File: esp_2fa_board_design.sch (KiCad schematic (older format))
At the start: 40 parts, among them IC1 TPS22919DCKR, J1 Conn_01x06_Female, J2 USB_C_Receptacle_USB2.0, Q1 DMP2045U-7, SW1 SW_Push, SW2 SW_Push, SW3 BOOT, SW4 RESET, U1 ESP32-WROOM-32, U2 DS3231M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

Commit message: Updated schematics - removed coin cell charging circuit
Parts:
- removed D1: 1N4148, Diode_THT:D_DO-35_SOD27_P7.62mm_Horizontal, symbol esp_2fa_board_design-rescue:1N4148-Diode
- removed R4: 200, Resistor_SMD:R_2816_7142Metric_Pad3.20x4.45mm_HandSolder, symbol esp_2fa_board_design-rescue:R_Small_US-Device
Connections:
- wire segments 164 -> 160
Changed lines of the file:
@@
 $EndDescr
-$Comp
-L esp_2fa_board_design-rescue:R_Small_US-Device R4
-U 1 1 5F5143E7
-P 9650 1350
-F 0 "R4" V 9550 1350 50  0000 C CNN
-F 1 "200" V 9764 1350 50  0000 C CNN
-F 2 "Resistor_SMD:R_2816_7142Metric_Pad3.20x4.45mm_HandSolder" H 9650 1350 50  0001 C CNN
-F 3 "~" H 9650 1350 50  0001 C CNN
-	1    9650 1350
-	0    -1   -1   0
-$EndComp
 $Comp
 L esp_2fa_board_design-rescue:C-Device C2
@@
 Wire Wire Line
 	8800 1650 8800 1900
-$Comp
-L esp_2fa_board_design-rescue:1N4148-Diode D1
-U 1 1 5F5151C5
-P 9200 1350
-F 0 "D1" H 9100 1300 50  0000 C CNN
-F 1 "1N4148" H 9200 1450 50  0000 C CNN
-F 2 "Diode_THT:D_DO-35_SOD27_P7.62mm_Horizontal" H 9200 1175 50  0001 C CNN
-F 3 "https://assets.nexperia.com/documents/data-sheet/1N4148_1N4448.pdf" H 9200 1350 50  0001 C CNN
-	1    9200 1350
-	1    0    0    -1
-$EndComp
-Wire Wire Line
-	9350 1350 9550 1350
-Wire Wire Line
-	9050 1350 8800 1350
-Wire Wire Line
-	8800 1350 8800 1650
-Connection ~ 8800 1650
-Wire Wire Line
-	9950 1350 9750 1350
 Wire Wire Line
 	9550 3500 9800 3500
@@
 Text Label 7200 1300 2    50   ~ 0
 LOAD_SWITCH_VCC
-Text Label 9950 1350 0    50   ~ 0
-LOAD_SWITCH_VCC
-Wire Wire Line
+Wire Wire Line

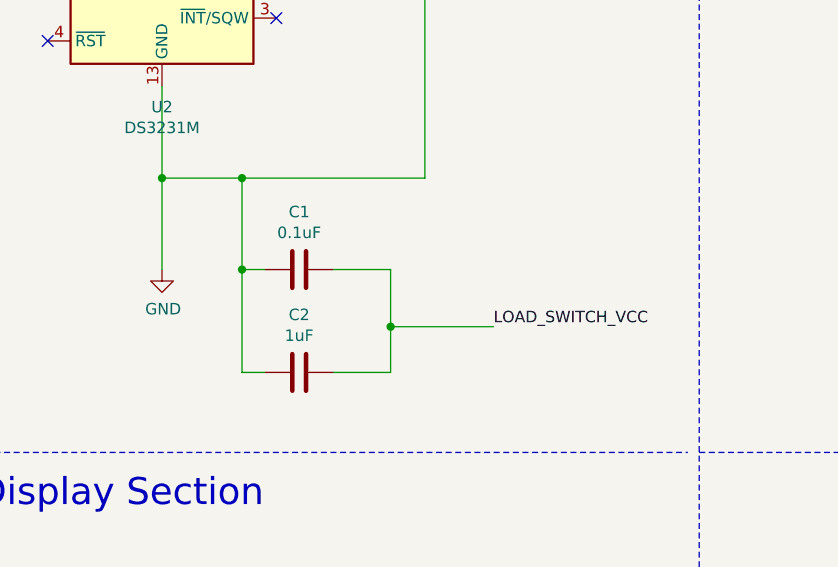
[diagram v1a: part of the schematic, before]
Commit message: Removed redundant rcapaciors
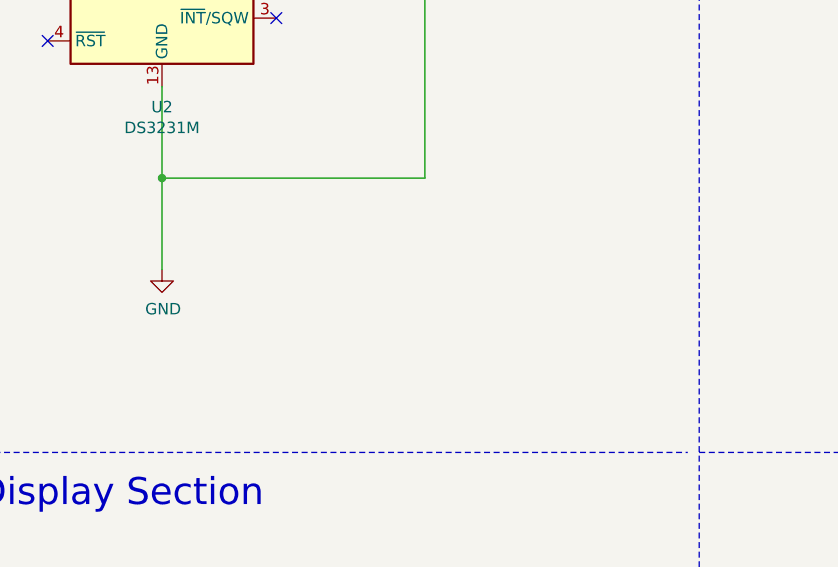
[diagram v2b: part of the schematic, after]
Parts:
- removed C1: 0.1uF, Capacitor_SMD:C_2816_7142Metric_Pad3.20x4.45mm_HandSolder, symbol esp_2fa_board_design-rescue:C-Device
- removed C2: 1uF, Capacitor_SMD:C_2816_7142Metric_Pad3.20x4.45mm_HandSolder, symbol esp_2fa_board_design-rescue:C-Device
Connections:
- wire segments 160 -> 150
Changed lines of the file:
@@
 Comment4 "Author: Vedant Paranjape"
 $EndDescr
-$Comp
-L esp_2fa_board_design-rescue:C-Device C2
-U 1 1 5F4FB645
-P 9400 3950
-F 0 "C2" V 9148 3950 50  0000 C CNN
-F 1 "1uF" V 9239 3950 50  0000 C CNN
-F 2 "Capacitor_SMD:C_2816_7142Metric_Pad3.20x4.45mm_HandSolder" H 9438 3800 50  0001 C CNN
-F 3 "~" H 9400 3950 50  0001 C CNN
-	1    9400 3950
-	0    1    1    0
-$EndComp
-$Comp
-L esp_2fa_board_design-rescue:C-Device C1
-U 1 1 5F4FA4EC
-P 9400 3500
-F 0 "C1" V 9148 3500 50  0000 C CNN
-F 1 "0.1uF" V 9239 3500 50  0000 C CNN
-F 2 "Capacitor_SMD:C_2816_7142Metric_Pad3.20x4.45mm_HandSolder" H 9438 3350 50  0001 C CNN
-F 3 "~" H 9400 3500 50  0001 C CNN
-	1    9400 3500
-	0    1    1    0
-$EndComp
 Wire Wire Line
 	7600 2000 7600 2200
@@
 	8800 2700 8800 3100
 Wire Wire Line
-	8800 3100 9150 3100
-Wire Wire Line
 	9950 3100 9950 2050
 Wire Wire Line
@@
 Wire Wire Line
 	8800 1650 8800 1900
-Wire Wire Line
-	9550 3500 9800 3500
-Wire Wire Line
-	9550 3950 9800 3950
-Wire Wire Line
-	9250 3500 9150 3500
-Wire Wire Line
-	9150 3500 9150 3950
-Wire Wire Line
-	9150 3950 9250 3950
-Wire Wire Line
-	9150 3100 9150 3500
-Connection ~ 9150 3100
-Wire Wire Line
-	9150 3100 9950 3100
-Connection ~ 9150 3500
 Wire Wire Line
 	2850 2950 3200 2950
@@
 Wire Wire Line
 	7800 1300 7800 1800
-Wire Wire Line
-	9800 3500 9800 3750
-Wire Wire Line
-	9800 3750 10250 3750
-Connection ~ 9800 3750
-Wire Wire Line
-	9800 3750 9800 3950
-Text Label 10250 3750 0    50   ~ 0
-LOAD_SWITCH_VCC
 Wire Wire Line
 	7800 1300 7200 1300
@@
 Wire Wire Line
 	14050 8800 14500 8800
+Wire Wire Line
+	8800 3100 9950 3100
 $EndSCHEMATC

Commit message: Completed footprint association and generated Bill of materials
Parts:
- removed J2: USB_C_Receptacle_USB2.0, symbol esp_2fa_board_design-rescue:USB_C_Receptacle_USB2.0-Connector
- added J2: TYPE-C-31-M-17, TYPE-C-31-M-17:TYPEC31M17, symbol TYPE-C-31-M-17:TYPE-C-31-M-17
- BT1: footprint Battery:Battery_Panasonic_CR2032-VS1N_Vertical_CircularHoles -> BU2032SM-BT-GTR:BU2032SMBTGTR
- C3, C4, C5: footprint Capacitor_SMD:C_2816_7142Metric_Pad3.20x4.45mm_HandSolder -> Capacitor_SMD:C_1206_3216Metric
- C6, C7, C8, C9: footprint (none) -> Capacitor_SMD:C_1206_3216Metric
- D2: footprint (none) -> LED_SMD:LED_0603_1608Metric_Castellated
- D3: footprint Diode_THT:D_DO-41_SOD81_P10.16mm_Horizontal -> Diode_SMD:D_SOD-123
- IC1: footprint SOT65P210X110-6N -> TPS22919DCKR:SOT65P210X110-6N
- L1: value INDUCTOR -> 2.2 uH; footprint (none) -> CDRH104RNP-150NC:INDPM102100X400N
- Q1: footprint SOT96P240X110-3N -> DMP2045U-7:SOT96P240X110-3N
- R1, R11, R12, R13: footprint (none) -> Resistor_SMD:R_0603_1608Metric
- R10, R2, R3, R5, R6, R8, R9: footprint Resistor_SMD:R_2816_7142Metric_Pad3.20x4.45mm_HandSolder -> Resistor_SMD:R_0603_1608Metric
- R7: value 4700 -> 4.7k; footprint Resistor_SMD:R_2816_7142Metric_Pad3.20x4.45mm_HandSolder -> Resistor_SMD:R_0603_1608Metric
- SW1, SW2, SW3, SW4: footprint Button_Switch_SMD:SW_SPST_B3S-1100 -> Button_Switch_SMD:SW_Push_1P1T_NO_6x6mm_H9.5mm
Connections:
- wire segments 150 -> 154
- no-connect marks 34 -> 32
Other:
- moved on the sheet: R11, R12

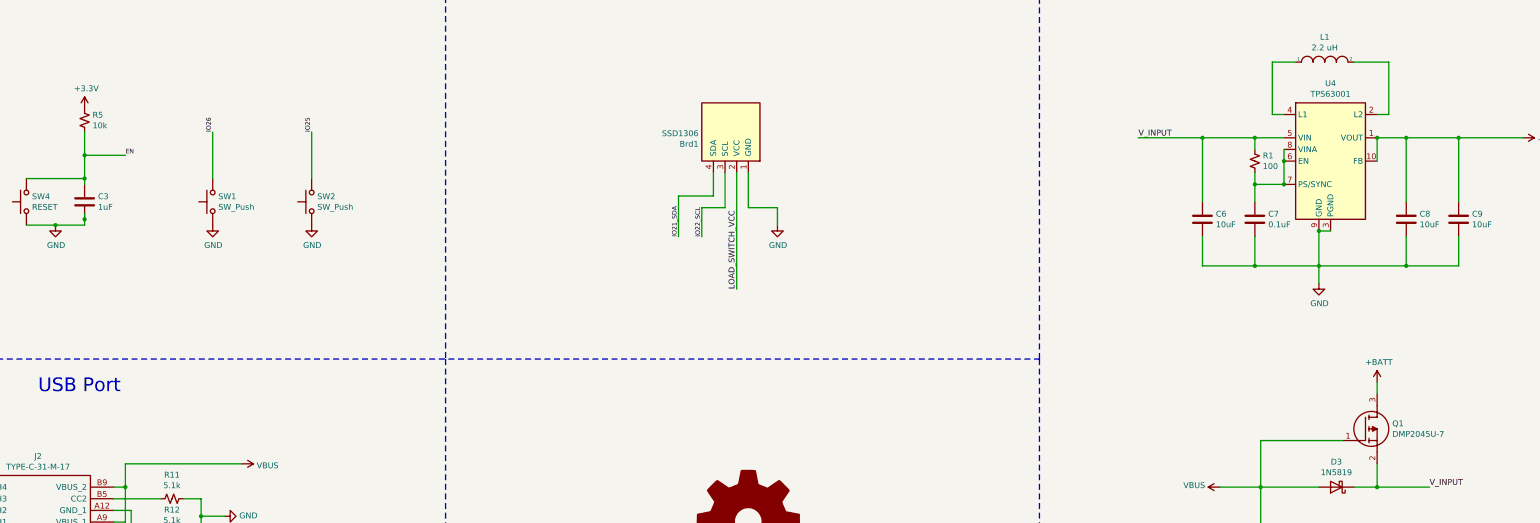
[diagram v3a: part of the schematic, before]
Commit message: Changed dmp2045u with cheaper dmp2305u and added pull resistor to switches
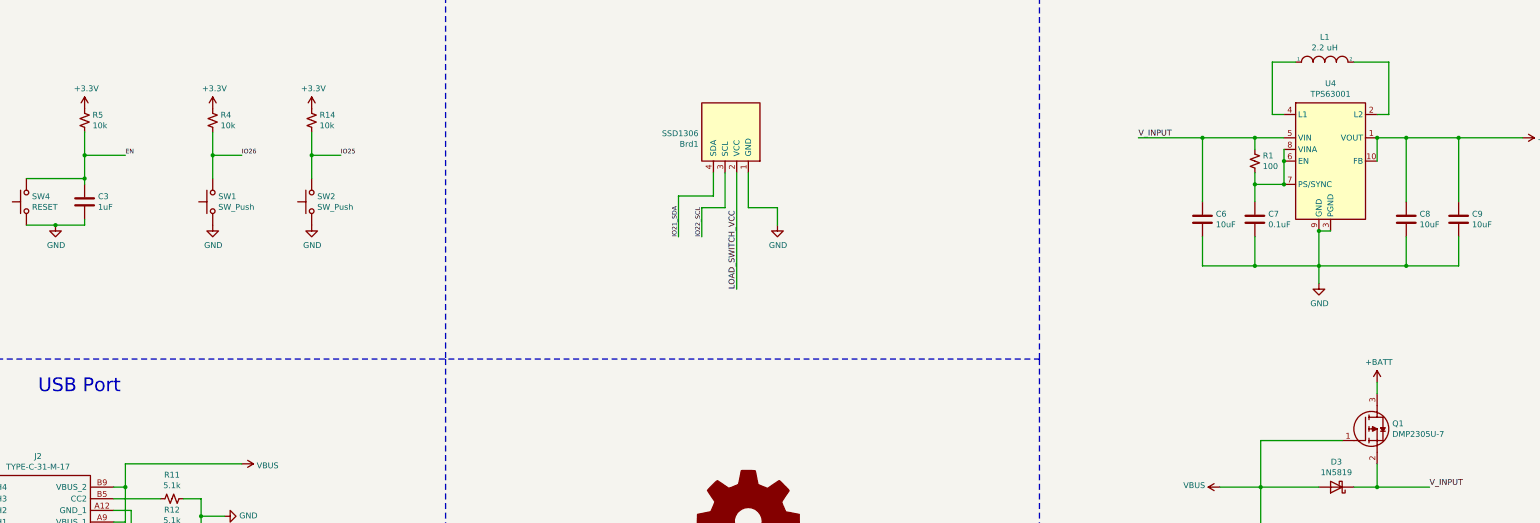
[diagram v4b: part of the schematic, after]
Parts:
- removed Q1: DMP2045U-7, DMP2045U-7:SOT96P240X110-3N, symbol DMP2045U-7:DMP2045U-7
- added Q1: DMP2305U-7, DMP2305U-7:SOT96P240X110-3N, symbol DMP2305U-7:DMP2305U-7
- added R14, R4: 10k, Resistor_SMD:R_0603_1608Metric, symbol esp_2fa_board_design-rescue:R_Small_US-Device
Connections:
- net +3V3: now also R14.1, R4.1
- net +BATT: now also Q1.3
- net IO25: now also R14.2
- net IO26: now also R4.2
- net VBUS: now also Q1.1
- net V_INPUT: now also Q1.2
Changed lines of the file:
@@
 	2950 6550 2700 6550
-Wire Wire Line
-	2950 6450 2950 6500
-Connection ~ 2950 6500
 Wire Wire Line
 	2950 6500 2950 6550
@@
 	2850 3150 3200 3150
 Wire Wire Line
-	4050 6150 4050 5750
+	4050 6150 4050 5950
 Text Label 3200 3150 0    39   ~ 0
 IO26
-Text Label 4050 5750 1    39   ~ 0
+Text Label 4300 5950 0    39   ~ 0
 IO26
 Wire Wire Line
@@
 IO25
 Wire Wire Line
-	4900 6150 4900 5750
-Text Label 4900 5750 1    39   ~ 0
+	4900 6150 4900 5950
+Text Label 5150 5950 0    39   ~ 0
 IO25
 Wire Wire Line
@@
 Wire Wire Line
 	13050 9350 13050 9550
-$Comp
-L DMP2045U-7:DMP2045U-7 Q1
-U 1 1 5FD513CE
-P 13750 8400
-F 0 "Q1" H 14180 8546 50  0000 L CNN
-F 1 "DMP2045U-7" H 14180 8455 50  0000 L CNN
-F 2 "DMP2045U-7:SOT96P240X110-3N" H 14200 8350 50  0001 L CNN
-F 3 "https://www.diodes.com/assets/Datasheets/DMP2045U.pdf" H 14200 8250 50  0001 L CNN
-F 4 "DMP2045U-7 P-Channel MOSFET, 3.5 (State) A, 4.3 (Steady) A, 20 V, 3-Pin SOT-23 Diodes Inc" H 14200 8150 50  0001 L CNN "Description"
-F 5 "1.1" H 14200 8050 50  0001 L CNN "Height"
-F 6 "Diodes Inc." H 14200 7950 50  0001 L CNN "Manufacturer_Name"
-F 7 "DMP2045U-7" H 14200 7850 50  0001 L CNN "Manufacturer_Part_Number"
-F 8 "DMP2045U-7" H 14200 7750 50  0001 L CNN "Arrow Part Number"
-F 9 "https://www.arrow.com/en/products/dmp2045u-7/diodes-incorporated" H 14200 7650 50  0001 L CNN "Arrow Price/Stock"
-F 10 "621-DMP2045U-7" H 14200 7550 50  0001 L CNN "Mouser Part Number"
-F 11 "https://www.mouser.co.uk/ProductDetail/Diodes-Incorporated/DMP2045U-7?qs=rrS6PyfT74erdUwo5CgHTg%3D%3D" H 14200 7450 50  0001 L CNN "Mouser Price/Stock"
-	1    13750 8400
-	1    0    0    -1
-$EndComp
 Wire Wire Line
 	14050 8000 14050 7900
@@
 NoConn ~ 1900 9000
 NoConn ~ 1900 9100
+$Comp
+L DMP2305U-7:DMP2305U-7 Q1
+U 1 1 5FB76610
+P 13750 8400
+F 0 "Q1" H 14180 8546 50  0000 L CNN
+F 1 "DMP2305U-7" H 14180 8455 50  0000 L CNN
+F 2 "DMP2305U-7:SOT96P240X110-3N" H 14200 8350 50  0001 L CNN
+F 3 "http://www.diodes.com/_files/datasheets/ds31737.pdf" H 14200 8250 50  0001 L CNN
+F 4 "MOSFET P-Channel 20V 4.2A SOT23 Diodes Inc DMP2305U-7 P-channel MOSFET Transistor, 4.2 A, -20 V, 3-Pin SOT-23" H 14200 8150 50  0001 L CNN "Description"
+F 5 "1.1" H 14200 8050 50  0001 L CNN "Height"
+F 6 "Diodes Inc." H 14200 7950 50  0001 L CNN "Manufacturer_Name"
+F 7 "DMP2305U-7" H 14200 7850 50  0001 L CNN "Manufacturer_Part_Number"
+F 8 "DMP2305U-7" H 14200 7750 50  0001 L CNN "Arrow Part Number"
+F 9 "https://www.arrow.com/en/products/dmp2305u-7/diodes-incorporated" H 14200 7650 50  0001 L CNN "Arrow Price/Stock"
+F 10 "621-DMP2305U-7" H 14200 7550 50  0001 L CNN "Mouser Part Number"
+F 11 "https://www.mouser.co.uk/ProductDetail/Diodes-Incorporated/DMP2305U-7?qs=oUsD4qhOtFyFQmlG8wLVjw%3D%3D" H 14200 7450 50  0001 L CNN "Mouser Price/Stock"
+	1    13750 8400
+	1    0    0    -1
+$EndComp
+$Comp
+L esp_2fa_board_design-rescue:R_Small_US-Device R4
+U 1 1 5FB7C439
+P 4050 5650
+F 0 "R4" H 4118 5696 50  0000 L CNN
+F 1 "10k" H 4118 5605 50  0000 L CNN
+F 2 "Resistor_SMD:R_0603_1608Metric" H 4050 5650 50  0001 C CNN
+F 3 "~" H 4050 5650 50  0001 C CNN
+	1    4050 5650
+	1    0    0    -1
+$EndComp
+$Comp
+L esp_2fa_board_design-rescue:R_Small_US-Device R14
+U 1 1 5FB7C8DA
+P 4900 5650
+F 0 "R14" H 4968 5696 50  0000 L CNN
+F 1 "10k" H 4968 5605 50  0000 L CNN
+F 2 "Resistor_SMD:R_0603_1608Metric" H 4900 5650 50  0001 C CNN
+F 3 "~" H 4900 5650 50  0001 C CNN
+	1    4900 5650
+	1    0    0    -1
+$EndComp
+$Comp
+L esp_2fa_board_design-rescue:+3.3V-power #PWR028
+U 1 1 5FB81EE2
+P 4050 5550
+F 0 "#PWR028" H 4050 5400 50  0001 C CNN
+F 1 "+3.3V" H 4065 5723 50  0000 C CNN
+F 2 "" H 4050 5550 50  0001 C CNN
+F 3 "" H 4050 5550 50  0001 C CNN
+	1    4050 5550
+	1    0    0    -1
+$EndComp
+$Comp
+L esp_2fa_board_design-rescue:+3.3V-power #PWR029
+U 1 1 5FB822F3
+P 4900 5550
+F 0 "#PWR029" H 4900 5400 50  0001 C CNN
+F 1 "+3.3V" H 4915 5723 50  0000 C CNN
+F 2 "" H 4900 5550 50  0001 C CNN
+F 3 "" H 4900 5550 50  0001 C CNN
+	1    4900 5550
+	1    0    0    -1
+$EndComp
+Wire Wire Line
+	4050 5950 4300 5950
+Connection ~ 4050 5950
+Wire Wire Line
+	4050 5950 4050 5750
+Wire Wire Line
+	4900 5950 5150 5950
+Connection ~ 4900 5950
+Wire Wire Line
+	4900 5950 4900 5750
 $EndSCHEMATC

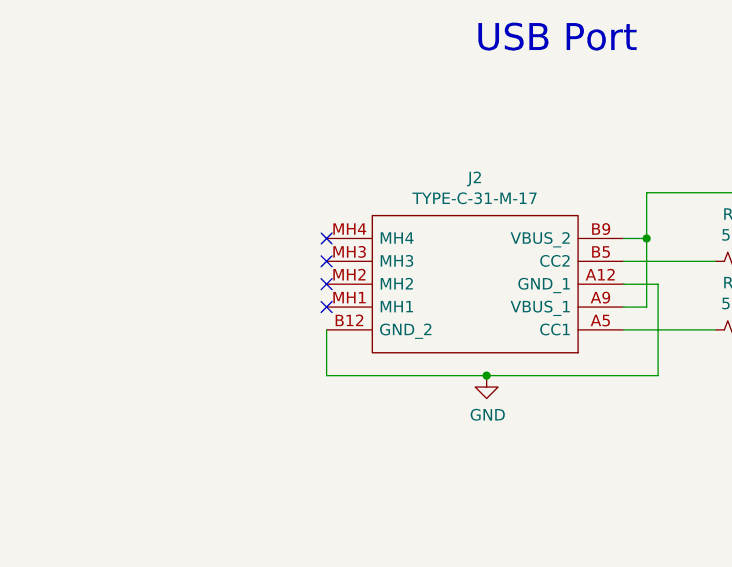
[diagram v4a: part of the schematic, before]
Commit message: Started layout of components. Fixed the Edge cut of PCB and rough location of components. Routing is yet to be done
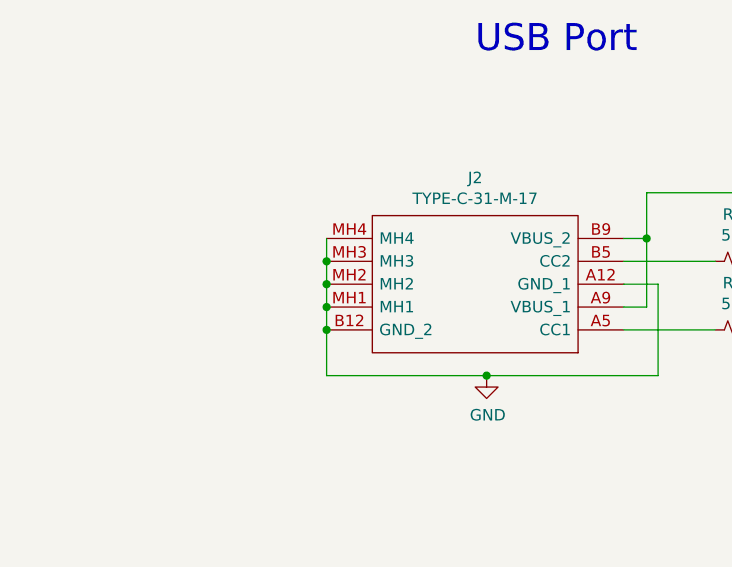
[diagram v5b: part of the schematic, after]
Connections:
- net GND: now also J2.MH1, J2.MH2, J2.MH3, J2.MH4
- no-connect marks 32 -> 28
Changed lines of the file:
@@
 Wire Wire Line
 	8800 3100 9950 3100
-$Comp
-L TYPE-C-31-M-17:TYPE-C-31-M-17 J2
-U 1 1 5FB28BF9
-P 3200 9200
-F 0 "J2" H 3850 8535 50  0000 C CNN
-F 1 "TYPE-C-31-M-17" H 3850 8626 50  0000 C CNN
-F 2 "TYPE-C-31-M-17:TYPEC31M17" H 4350 9300 50  0001 L CNN
-F 3 "https://datasheet.lcsc.com/szlcsc/1903211732_Korean-Hroparts-Elec-TYPE-C-31-M-17_C283540.pdf" H 4350 9200 50  0001 L CNN
-F 4 "USB Connectors 6 Receptacle 1 RoHS" H 4350 9100 50  0001 L CNN "Description"
-F 5 "3.26" H 4350 9000 50  0001 L CNN "Height"
-F 6 "Korean Hroparts Elec" H 4350 8900 50  0001 L CNN "Manufacturer_Name"
-F 7 "TYPE-C-31-M-17" H 4350 8800 50  0001 L CNN "Manufacturer_Part_Number"
-F 8 "" H 4350 8700 50  0001 L CNN "Arrow Part Number"
-F 9 "" H 4350 8600 50  0001 L CNN "Arrow Price/Stock"
-F 10 "" H 4350 8500 50  0001 L CNN "Mouser Part Number"
-F 11 "" H 4350 8400 50  0001 L CNN "Mouser Price/Stock"
-	1    3200 9200
-	-1   0    0    1
-$EndComp
 Wire Wire Line
 	3800 9200 3950 9200
@@
 Wire Wire Line
 	2600 9400 1900 9400
-NoConn ~ 1900 8800
-NoConn ~ 1900 8900
-NoConn ~ 1900 9000
-NoConn ~ 1900 9100
 $Comp
 L DMP2305U-7:DMP2305U-7 Q1
@@
 Wire Wire Line
 	4900 5950 4900 5750
+$Comp
+L TYPE-C-31-M-17:TYPE-C-31-M-17 J2
+U 1 1 5FB28BF9
+P 3200 9200
+F 0 "J2" H 3850 8535 50  0000 C CNN
+F 1 "TYPE-C-31-M-17" H 3850 8626 50  0000 C CNN
+F 2 "TYPE-C-31-M-17:TYPEC31M17" H 4350 9300 50  0001 L CNN
+F 3 "https://datasheet.lcsc.com/szlcsc/1903211732_Korean-Hroparts-Elec-TYPE-C-31-M-17_C283540.pdf" H 4350 9200 50  0001 L CNN
+F 4 "USB Connectors 6 Receptacle 1 RoHS" H 4350 9100 50  0001 L CNN "Description"
+F 5 "3.26" H 4350 9000 50  0001 L CNN "Height"
+F 6 "Korean Hroparts Elec" H 4350 8900 50  0001 L CNN "Manufacturer_Name"
+F 7 "TYPE-C-31-M-17" H 4350 8800 50  0001 L CNN "Manufacturer_Part_Number"
+F 8 "" H 4350 8700 50  0001 L CNN "Arrow Part Number"
+F 9 "" H 4350 8600 50  0001 L CNN "Arrow Price/Stock"
+F 10 "" H 4350 8500 50  0001 L CNN "Mouser Part Number"
+F 11 "" H 4350 8400 50  0001 L CNN "Mouser Price/Stock"
+	1    3200 9200
+	-1   0    0    1
+$EndComp
+Wire Wire Line
+	1900 8800 1900 8900
+Wire Wire Line
+	1900 8900 1900 9000
+Connection ~ 1900 8900
+Wire Wire Line
+	1900 9000 1900 9100
+Connection ~ 1900 9000
+Wire Wire Line
+	1900 9100 1900 9200
+Connection ~ 1900 9100
+Connection ~ 1900 9200
 $EndSCHEMATC
